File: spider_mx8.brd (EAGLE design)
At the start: 20 x 49.5 mm, 4 parts, among them IC1 AVR-MEGA8-PPTH, J1 AVR_SPI_PRG_6NS

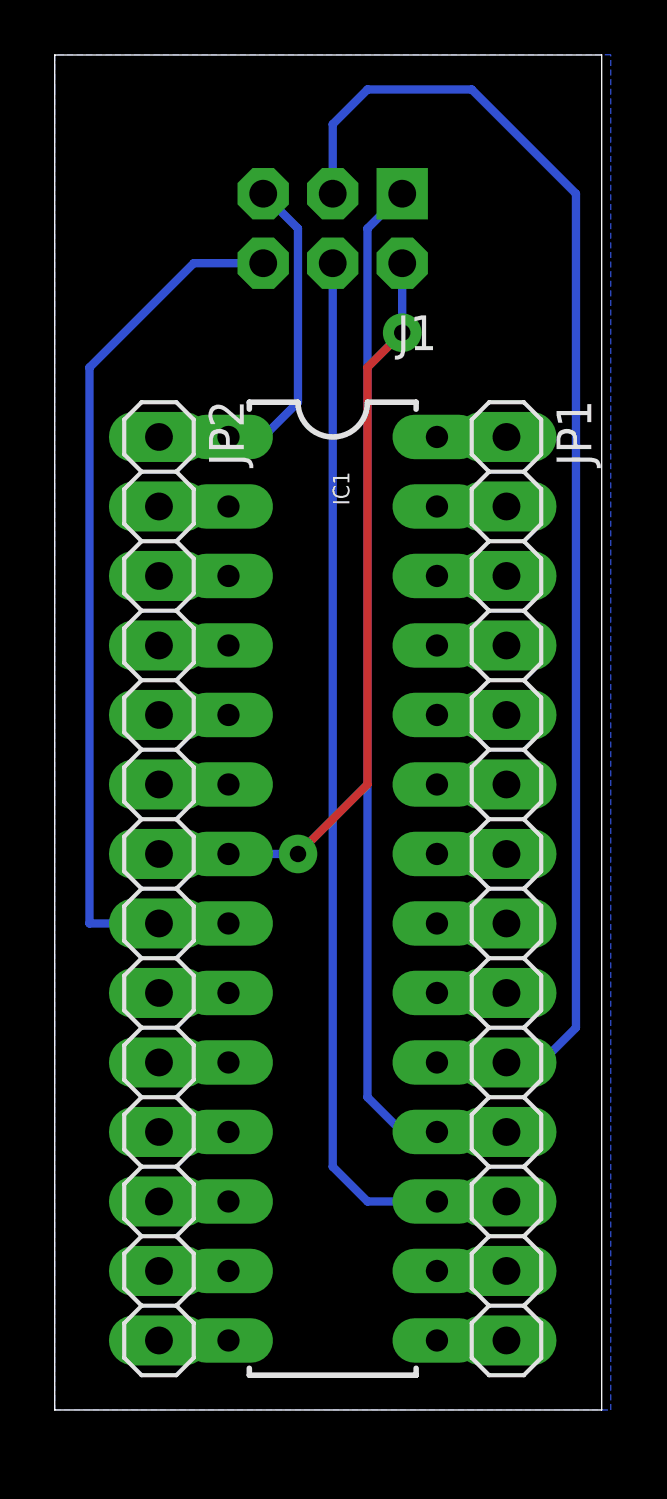
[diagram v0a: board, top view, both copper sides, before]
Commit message: added led and cap.  noticed all on bottom side
so I'll need to re-do all this with at least SMT parts on the top
if I want to keep it quasi-one-layer, I'll need to flip wires to top
too.  boo.
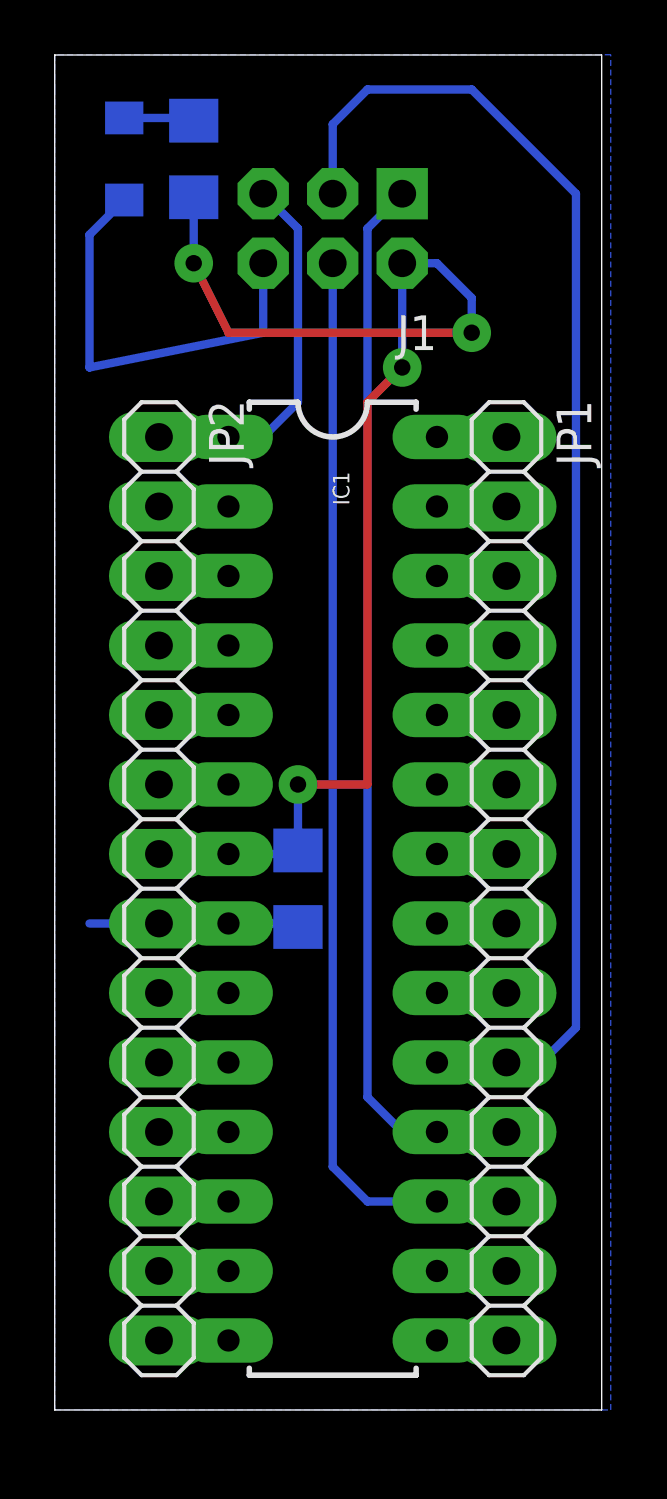
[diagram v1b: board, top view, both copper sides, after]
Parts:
- added C1: 0.1uF, SparkFun-Passives:1206
- added D1: Yellow, SparkFun-LED:LED-1206
- added R1: 1k Ohm, SparkFun-Passives:1206
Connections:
- new net N$14: D1.A, R1.2
- net GND: now also C1.2, D1.C
- net VCC: now also C1.1, R1.1
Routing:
- net VCC: track 28.2 -> 48.1 mm, vias 2 -> 4
- net GND: track 33.3 -> 23.3 mm
- net N$14: track 0.00 -> 2.58 mm
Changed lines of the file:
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@@
 <element name="JP1" library="pinhead" package="1X14" value="" x="49.53" y="36.83" rot="R270"/>
 <element name="JP2" library="pinhead" package="1X14" value="" x="36.83" y="36.83" rot="R270"/>
+<element name="R1" library="SparkFun-Passives" package="1206" value="1k Ohm" x="38.1" y="63.5" rot="MR90"/>
+<element name="D1" library="SparkFun-LED" package="LED-1206" value="Yellow" x="35.56" y="63.5" rot="MR270">
+<attribute name="PROD_ID" value="DIO-09909" x="39.37" y="63.5" size="1.778" layer="28" rot="MR270" display="off"/>
+</element>
+<element name="C1" library="SparkFun-Passives" package="1206" value="0.1uF" x="41.91" y="36.83" rot="MR270"/>
 </elements>
 <signals>
@@
 <contactref element="JP2" pad="7"/>
 <wire x1="36.83" y1="38.1" x2="39.37" y2="38.1" width="0.3048" layer="16"/>
-<wire x1="39.37" y1="38.1" x2="41.91" y2="38.1" width="0.3048" layer="16"/>
-<via x="41.91" y="38.1" extent="1-16" drill="0.6" shape="square"/>
-<wire x1="41.91" y1="38.1" x2="44.45" y2="40.64" width="0.3048" layer="1"/>
-<wire x1="44.45" y1="40.64" x2="44.45" y2="55.88" width="0.3048" layer="1"/>
-<wire x1="44.45" y1="55.88" x2="45.72" y2="57.15" width="0.3048" layer="1"/>
-<via x="45.72" y="57.15" extent="1-16" drill="0.6" shape="square"/>
-<wire x1="45.72" y1="57.15" x2="45.72" y2="59.69" width="0.3048" layer="16"/>
+<wire x1="44.45" y1="40.64" x2="44.45" y2="54.61" width="0.3048" layer="1"/>
+<wire x1="44.45" y1="54.61" x2="45.72" y2="55.88" width="0.3048" layer="1"/>
+<via x="45.72" y="55.88" extent="1-16" drill="0.6" shape="square"/>
+<wire x1="45.72" y1="55.88" x2="45.72" y2="59.69" width="0.3048" layer="16"/>
+<contactref element="R1" pad="1"/>
+<contactref element="C1" pad="1"/>
+<wire x1="44.45" y1="40.64" x2="41.91" y2="40.64" width="0.3048" layer="1"/>
+<via x="41.91" y="40.64" extent="1-16" drill="0.6" shape="square"/>
+<wire x1="41.91" y1="40.64" x2="41.91" y2="38.23" width="0.3048" layer="16"/>
+<wire x1="41.91" y1="38.23" x2="41.78" y2="38.1" width="0.3048" layer="16"/>
+<wire x1="41.78" y1="38.1" x2="39.37" y2="38.1" width="0.3048" layer="16"/>
+<wire x1="38.1" y1="62.1" x2="38.1" y2="59.69" width="0.3048" layer="16"/>
+<via x="38.1" y="59.69" extent="1-16" drill="0.6" shape="square"/>
+<wire x1="38.1" y1="59.69" x2="39.37" y2="57.15" width="0.3048" layer="1"/>
+<wire x1="39.37" y1="57.15" x2="48.26" y2="57.15" width="0.3048" layer="1"/>
+<via x="48.26" y="57.15" extent="1-16" drill="0.6" shape="square"/>
+<wire x1="48.26" y1="57.15" x2="48.26" y2="58.42" width="0.3048" layer="16"/>
+<wire x1="48.26" y1="58.42" x2="46.99" y2="59.69" width="0.3048" layer="16"/>
+<wire x1="46.99" y1="59.69" x2="45.72" y2="59.69" width="0.3048" layer="16"/>
 </signal>
 <signal name="GND">
@@
 <contactref element="J1" pad="6"/>
 <contactref element="JP2" pad="8"/>
-<polygon width="0.4064" layer="16">
+<polygon width="0.4064" layer="16" isolate="0.4064">
 <vertex x="33.02" y="66.04"/>
 <vertex x="33.02" y="17.78"/>
@@
 <vertex x="33.02" y="67.31"/>
 </polygon>
-<wire x1="40.64" y1="59.69" x2="38.1" y2="59.69" width="0.3048" layer="16"/>
-<wire x1="38.1" y1="59.69" x2="34.29" y2="55.88" width="0.3048" layer="16"/>
-<wire x1="34.29" y1="55.88" x2="34.29" y2="35.56" width="0.3048" layer="16"/>
+<wire x1="40.64" y1="59.69" x2="40.64" y2="57.15" width="0.3048" layer="16"/>
+<wire x1="40.64" y1="57.15" x2="34.29" y2="55.88" width="0.3048" layer="16"/>
 <wire x1="34.29" y1="35.56" x2="36.83" y2="35.56" width="0.3048" layer="16"/>
 <wire x1="36.83" y1="35.56" x2="39.37" y2="35.56" width="0.3048" layer="16"/>
+<contactref element="D1" pad="C"/>
+<contactref element="C1" pad="2"/>
+<wire x1="41.91" y1="35.43" x2="41.78" y2="35.56" width="0.3048" layer="16"/>
+<wire x1="41.78" y1="35.56" x2="39.37" y2="35.56" width="0.3048" layer="16"/>
+<wire x1="35.56" y1="62" x2="34.29" y2="60.73" width="0.3048" layer="16"/>
+<wire x1="34.29" y1="60.73" x2="34.29" y2="55.88" width="0.3048" layer="16"/>
+</signal>
+<signal name="N$14">
+<contactref element="R1" pad="2"/>
+<contactref element="D1" pad="A"/>
+<wire x1="38.1" y1="64.9" x2="38" y2="65" width="0.3048" layer="16"/>
+<wire x1="38" y1="65" x2="35.56" y2="65" width="0.3048" layer="16"/>
 </signal>
 </signals>

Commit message: moved everything to topside
still two vias, and has AVR footprint
next step, can I get a more compact layout by dropping the AVR?
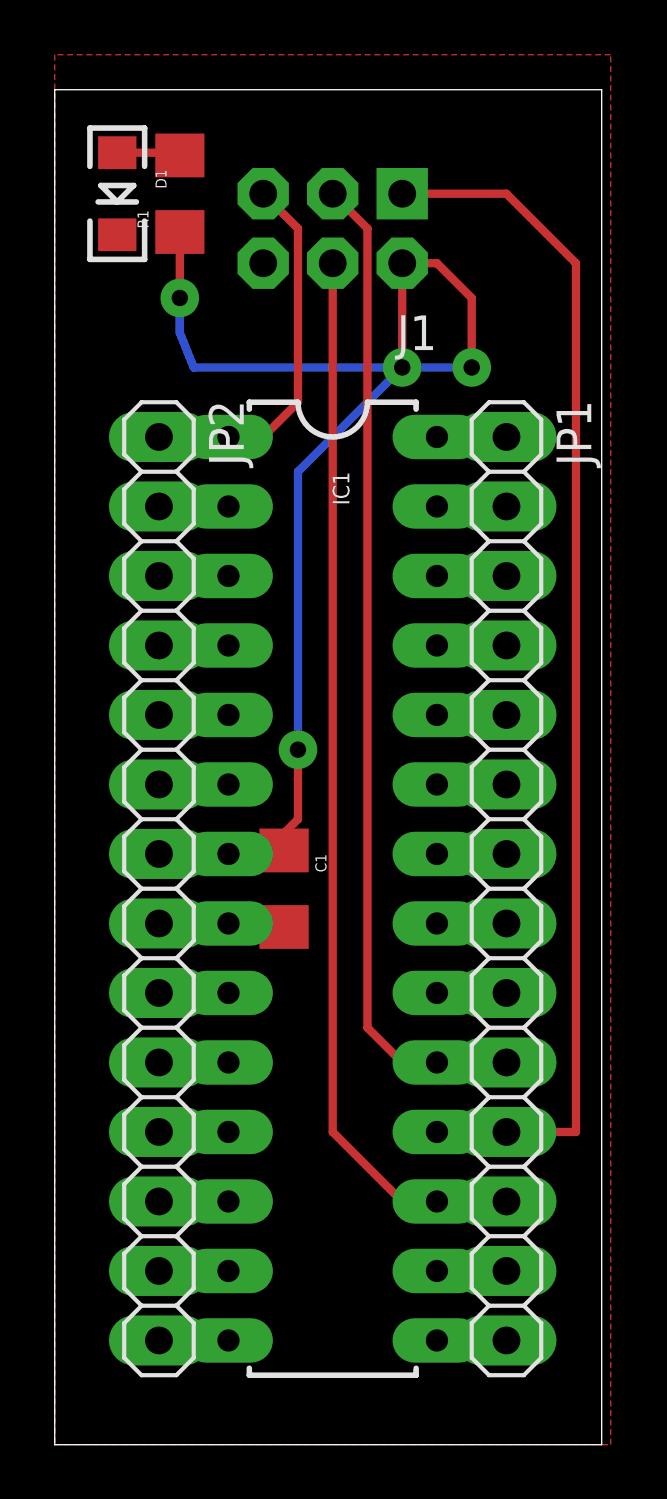
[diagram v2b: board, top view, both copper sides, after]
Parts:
- moved R1 1.37 mm to (37.6, 62.2), flipped to the top
- moved D1 1.30 mm to (35.3, 62.2), flipped to the top
- moved C1 0.51 mm to (41.4, 36.8), flipped to the top
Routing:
- net GND: track 23.3 -> 4.63 mm
- net SCK: track 49.6 -> 36.6 mm
- net MISO: track 39.2 -> 46.8 mm
- net MOSI: track 39.9 -> 39.2 mm
- net VCC: track 48.1 -> 48.7 mm
- added copper zone on layer 1, net GND
- removed copper zone on layer 16, net GND
